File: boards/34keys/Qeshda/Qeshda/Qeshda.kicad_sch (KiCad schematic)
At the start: 75 parts, among them J1 Conn_01x08_Female, SW1 SW_Push, SW10 SW_Push, SW11 SW_Push, SW12 SW_Push, SW13 SW_Push, SW14 SW_Push, SW15 SW_Push, SW16 SW_Push, SW17 SW_Push, SW18 SW_Push, SW19 SW_Push, SW2 SW_Push, SW20 SW_Push, SW21 SW_Push, SW22 SW_Push, SW23 SW_Push, SW24 SW_Push, SW25 SW_SPDT, SW26 Rotary_Encoder_Switch, SW27 SW_Push, SW28 SW_Push, SW29 SW_Push, SW3 SW_Push, SW30 SW_Push, SW31 SW_Push, SW32 SW_Push, SW34 SW_Push, SW37 SW_Push, SW38 SW_Push, SW39 SW_Push, SW4 SW_Push, SW40 SW_Push, SW5 SW_Push, SW6 SW_Push, SW7 SW_Push, SW8 SW_Push, SW9 SW_Push, U1 nice_nano

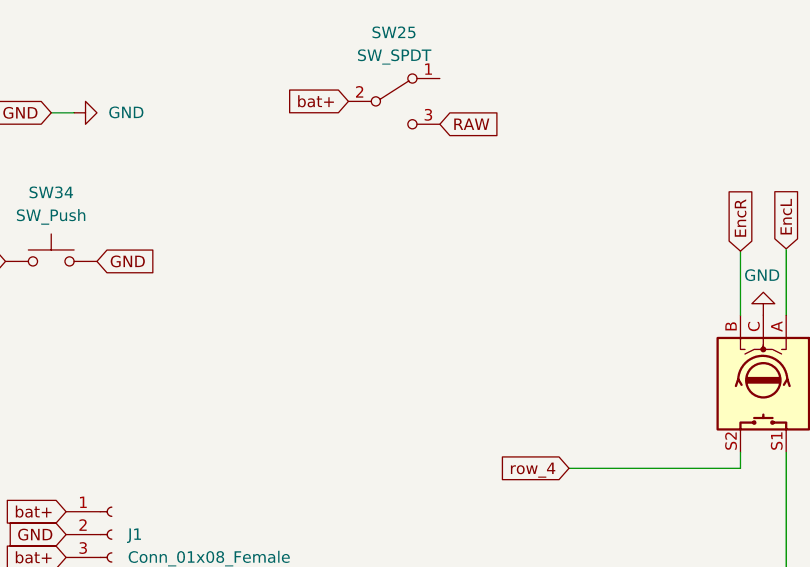
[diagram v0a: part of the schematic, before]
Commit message: More space for encoder in Qeschda
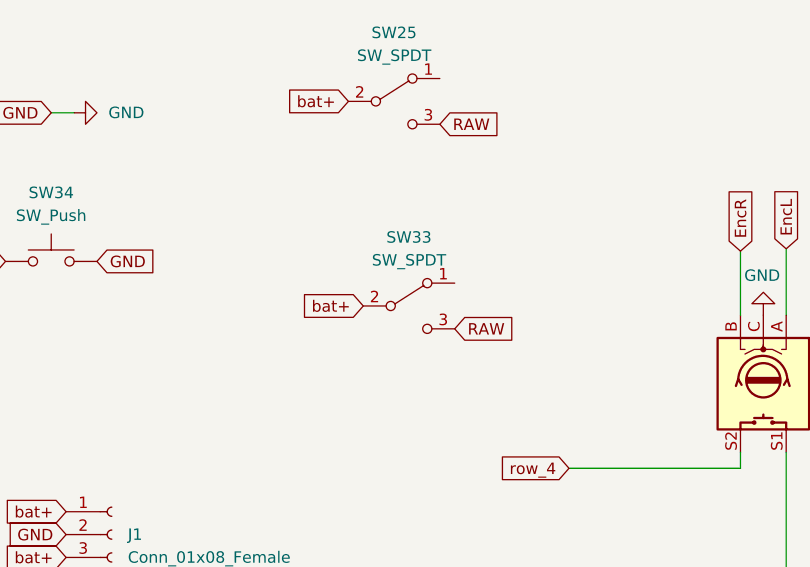
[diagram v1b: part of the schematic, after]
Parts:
- added SW33: SW_SPDT, Button_Switch_SMD:SW_SPDT_PCM12, symbol Switch:SW_SPDT
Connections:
- net RAW: now also SW33.3 (C)
- net bat+: now also SW33.2 (B)
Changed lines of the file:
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@@
+    )
+  )
+  (global_label "bat+" (shape input) (at 74.93 142.24 180) (fields_autoplaced)
+    (effects (font (size 1.27 1.27)) (justify right))
+    (property "Intersheetrefs" "${INTERSHEET_REFS}" (at 68.0604 142.1606 0)
+      (effects (font (size 1.27 1.27)) (justify right) hide)
     )
   )
@@
     (property "Intersheetrefs" "${INTERSHEET_REFS}" (at 66.4094 119.4276 0)
       (effects (font (size 1.27 1.27)) (justify right) hide)
+    )
+  )
+  (global_label "RAW" (shape input) (at 85.09 144.78 0) (fields_autoplaced)
+    (effects (font (size 1.27 1.27)) (justify left))
+    (property "Intersheetrefs" "${INTERSHEET_REFS}" (at 91.8058 144.78 0)
+      (effects (font (size 1.27 1.27)) (justify left) hide)
     )
   )
@@
         )
       )
+    )
+  )
+  (symbol (lib_id "Switch:SW_SPDT") (at 80.01 142.24 0) (unit 1)
+    (in_bom yes) (on_board yes) (dnp no) (fields_autoplaced)
+    (property "Reference" "SW33" (at 80.01 134.62 0)
+      (effects (font (size 1.27 1.27)))
+    )
+    (property "Value" "SW_SPDT" (at 80.01 137.16 0)
+      (effects (font (size 1.27 1.27)))
+    )
+    (property "Footprint" "Button_Switch_SMD:SW_SPDT_PCM12" (at 80.01 142.24 0)
+      (effects (font (size 1.27 1.27)) hide)
+    )
+    (property "Datasheet" "~" (at 80.01 142.24 0)
+      (effects (font (size 1.27 1.27)) hide)
+    )
+    (pin "1")
+    (pin "2")
+    (pin "3")
+    (instances
+      (project "Qeshda"
+        (path "/7618f2a4-24d4-4ffa-8830-ff7c23f32cea"
+          (reference "SW33") (unit 1)
+        )
+      )
+      (project "Bolbol"
+        (path "/eaef1172-3351-417c-bfc4-74a598f141cb"
+          (reference "SW34") (unit 1)
+        )
+      )
